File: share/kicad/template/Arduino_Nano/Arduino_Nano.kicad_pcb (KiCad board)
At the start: 2 copper layers, 17.8 x 43.2 mm, 6 parts, among them P1 Digital, P2 Analog, P3 CONN_01X01, P4 CONN_01X01, P5 CONN_01X01, P6 CONN_01X01

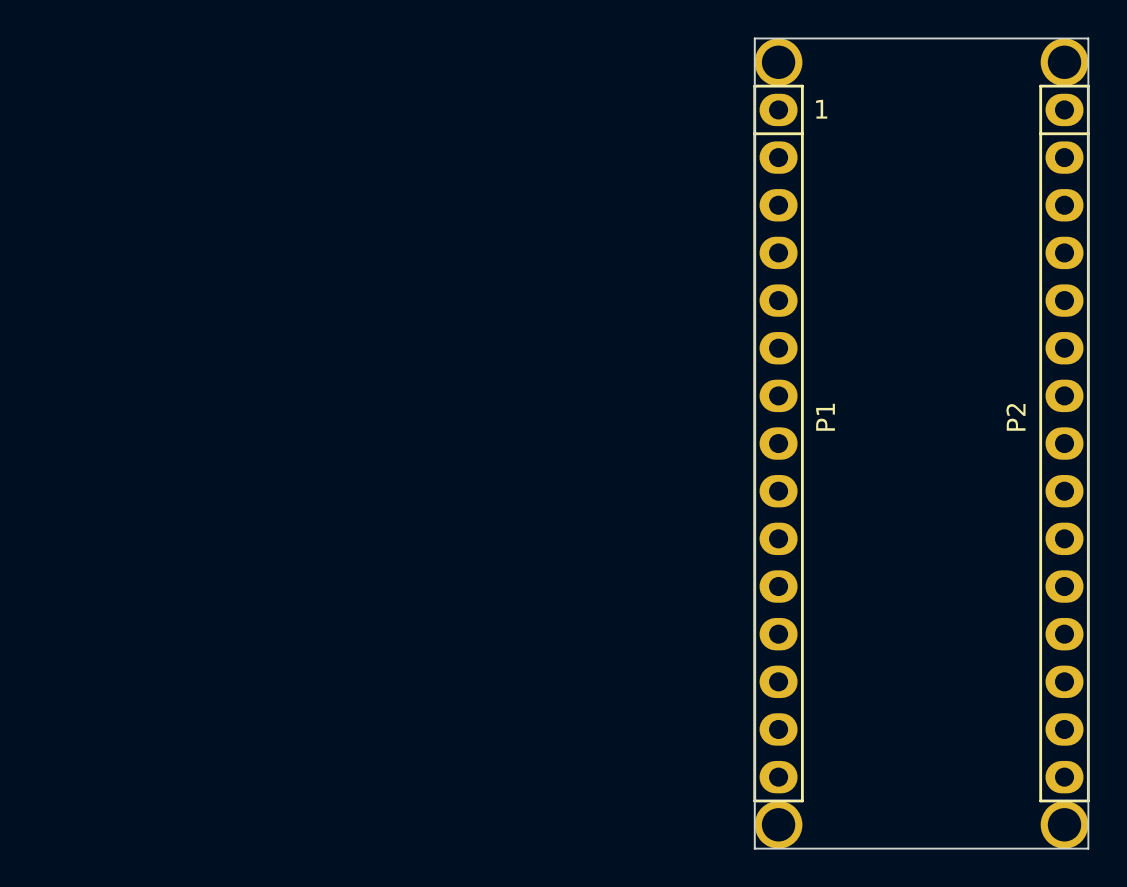
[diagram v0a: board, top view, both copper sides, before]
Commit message: Remove KiCad V4.0.7
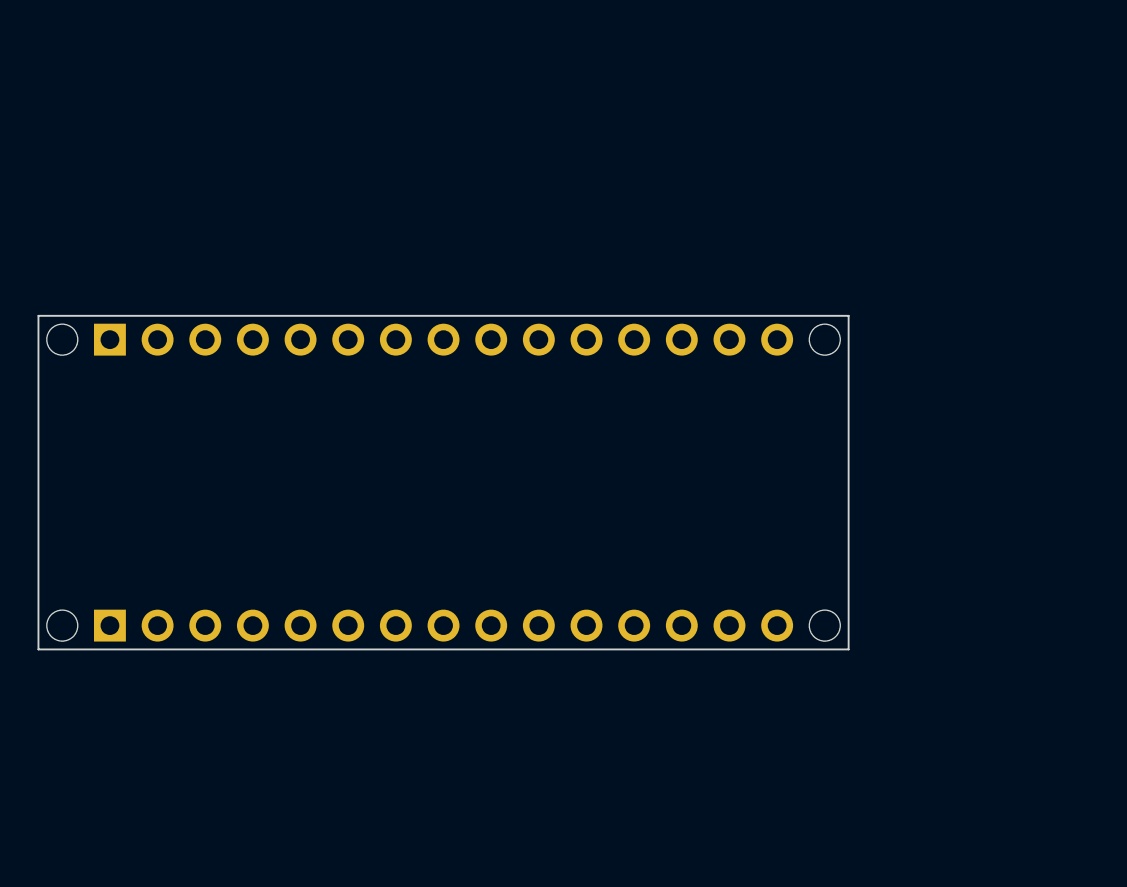
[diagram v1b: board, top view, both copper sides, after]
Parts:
- removed P1: Digital, Socket_Arduino_Nano:Socket_Strip_Arduino_1x15
- removed P2: Analog, Socket_Arduino_Nano:Socket_Strip_Arduino_1x15
- removed P3, P4, P5, P6: CONN_01X01, Socket_Arduino_Nano:1pin_Nano
- added J1: Analog, Connector_PinHeader_2.54mm:PinHeader_1x15_P2.54mm_Vertical, B.Cu at (103.8, 98.7)
- added J2: Digital, Connector_PinHeader_2.54mm:PinHeader_1x15_P2.54mm_Vertical, B.Cu at (103.8, 83.5)
- added MH1: MountingHole_65mil, Arduino_MountingHole:MountingHole_65mil, F.Cu at (101.3, 98.7)
- added MH2: MountingHole_65mil, Arduino_MountingHole:MountingHole_65mil, F.Cu at (101.3, 83.5)
- added MH3: MountingHole_65mil, Arduino_MountingHole:MountingHole_65mil, F.Cu at (141.9, 83.5)
- added MH4: MountingHole_65mil, Arduino_MountingHole:MountingHole_65mil, F.Cu at (141.9, 98.7)
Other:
- board size 17.8 x 43.2 mm -> 43.2 x 17.8 mm
- net class Default removed
- board text added: "ICSP"
- board text added: "USB Mini-B"
- board text removed: "1"
